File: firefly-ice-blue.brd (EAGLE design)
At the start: 34 x 33.5 mm, 119 parts, among them J1 USB-5PINMOLEX-47346, J2 CON-6SOCKET, U1 EFM32LG330F256, U10 STM6519, U11 TPS782XX, U12 TPS6208X, U13 NX3L1T53, U14 FDFMA2P029Z, U16 MEMORY-SPIWLBGA-8, U17 ADP151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

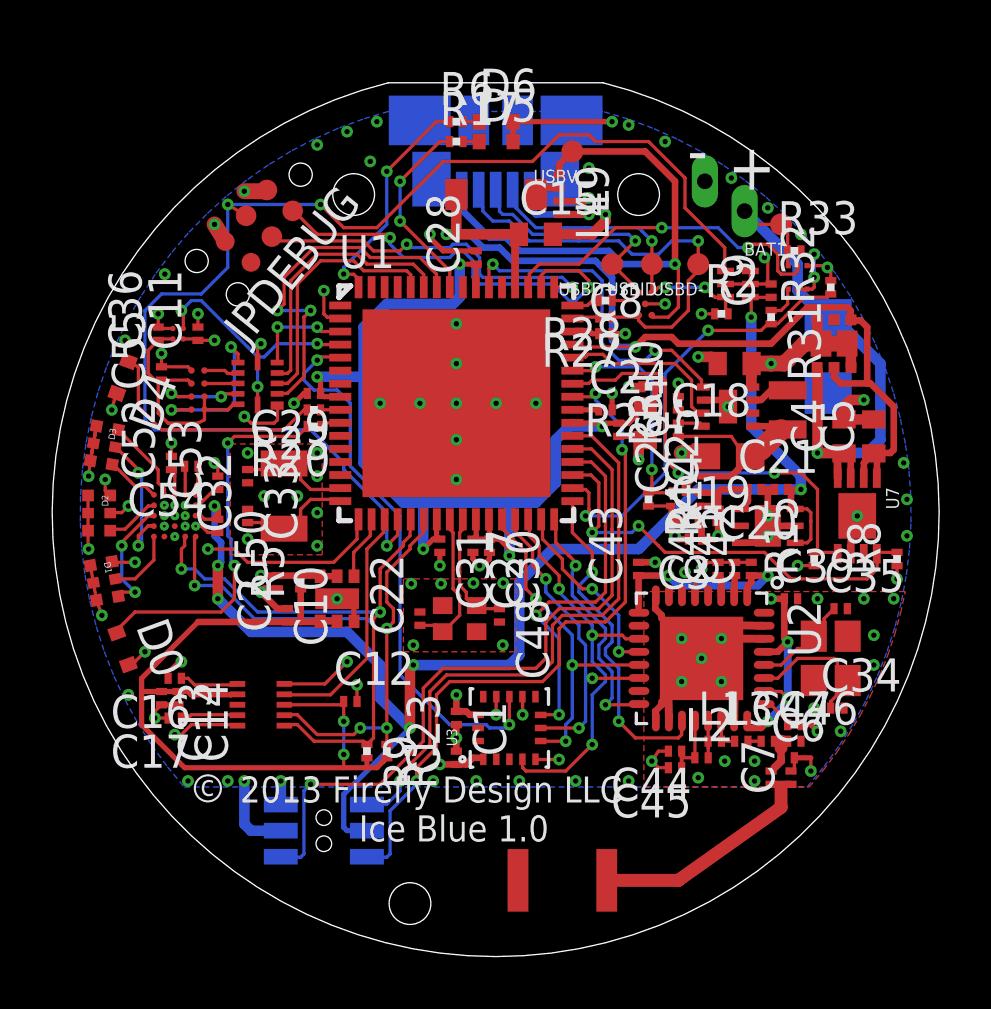
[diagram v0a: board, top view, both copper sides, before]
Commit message: fix reversed source/drain on p-channel mosfet of voltage sensing circuit
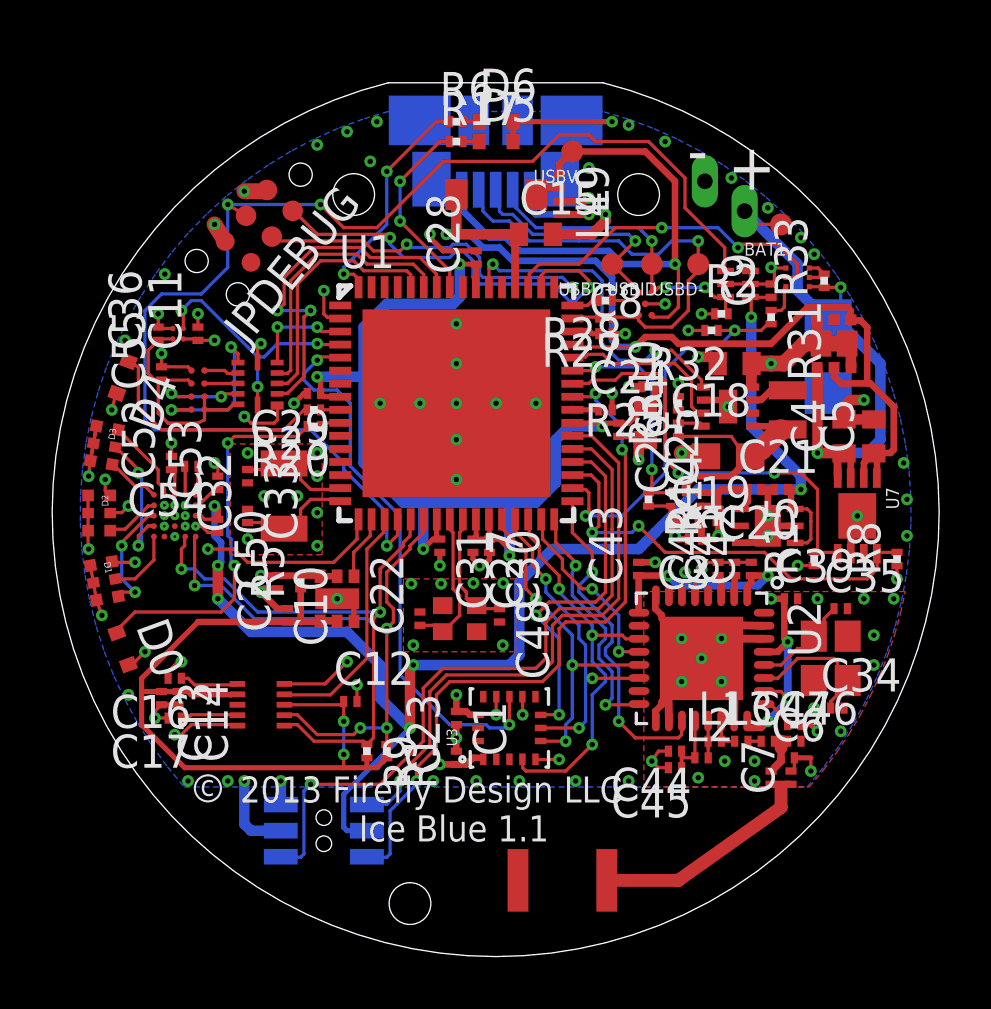
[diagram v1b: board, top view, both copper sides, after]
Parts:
- moved R32 4.86 mm to (25.3, 24.0), turned to 180 degrees
- moved R33 1.62 mm to (29.6, 25.9), turned to 90 degrees
- turned U6 to 0 degrees
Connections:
- net BAT_V: now also U6.4; no longer U6.3
- net N$60: now also U6.3; no longer U6.4
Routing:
- net BAT_V/2: track 16.8 -> 14.7 mm
- net BAT_V: track 24.1 -> 25.6 mm, vias 1 -> 2
- net N$45: track 2.57 -> 1.28 mm, vias 2 -> 0
- net GND: track 88.6 -> 88.3 mm, vias 115 -> 116
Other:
- board text added: "Ice Blue 1.1"
- board text removed: "Ice Blue 1.0"
